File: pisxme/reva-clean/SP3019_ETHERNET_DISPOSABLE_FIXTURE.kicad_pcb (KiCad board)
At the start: 6 copper layers, 300 x 180 mm, 4 parts, among them J2 A70-112-331N126, J7 Raspberry-Pi-5-Compute-Module, U6 SP3019-04HTG, U9 SP3019-04HTG

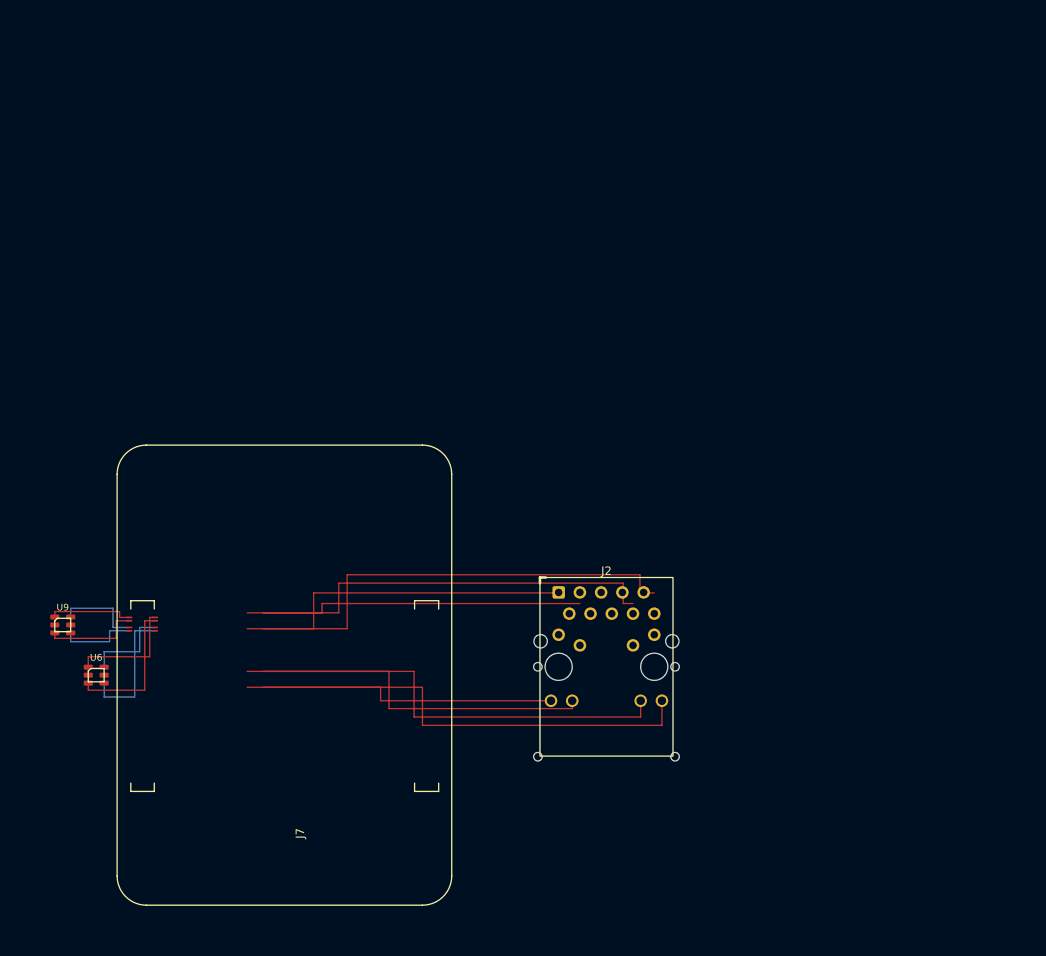
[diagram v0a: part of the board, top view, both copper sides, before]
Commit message: phase17: preserve reoriented Ethernet fixture trial
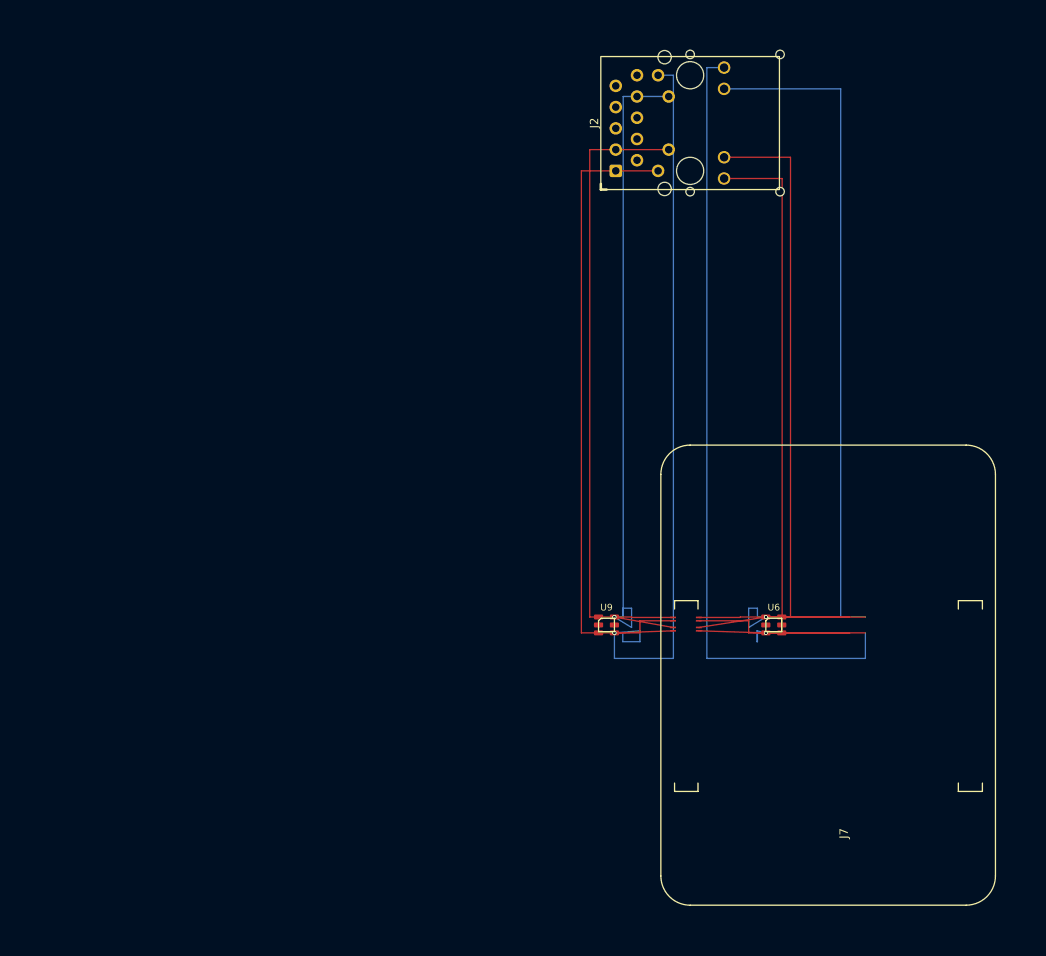
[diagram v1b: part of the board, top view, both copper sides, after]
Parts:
- moved U6 81.2 mm to (110.0, 100.0)
- moved J2 65.8 mm to (100.0, 40.0), turned to 90 degrees
- moved J7 65.0 mm to (100.0, 130.0)
- moved U9 65.0 mm to (90.0, 100.0)
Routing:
- net CM5_GBE_TD0_N: track 52.5 -> 107.8 mm, vias 0 -> 2
- net CM5_GBE_TD0_P: track 81.6 -> 119.1 mm, vias 0 -> 2
- net CM5_GBE_TD1_N: track 55.1 -> 88.8 mm
- net CM5_GBE_TD2_P: track 64.7 -> 97.1 mm, vias 0 -> 2
- net CM5_GBE_TD1_P: track 58.2 -> 88.0 mm
- net CM5_GBE_TD3_P: track 51.1 -> 75.3 mm
- net CM5_GBE_TD3_N: track 53.2 -> 76.8 mm
- net CM5_GBE_TD2_N: track 60.6 -> 83.6 mm, vias 0 -> 2

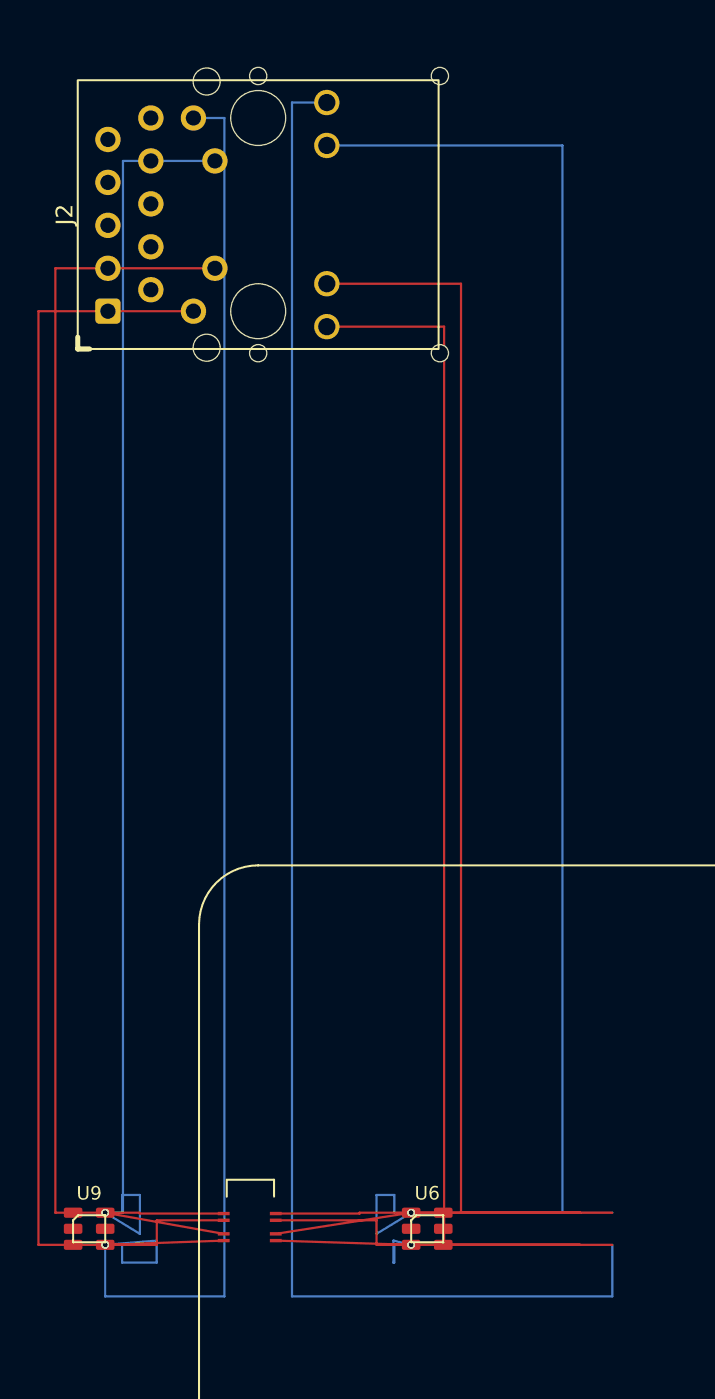
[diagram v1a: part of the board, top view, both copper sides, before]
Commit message: phase17: preserve explicit Ethernet transition trial
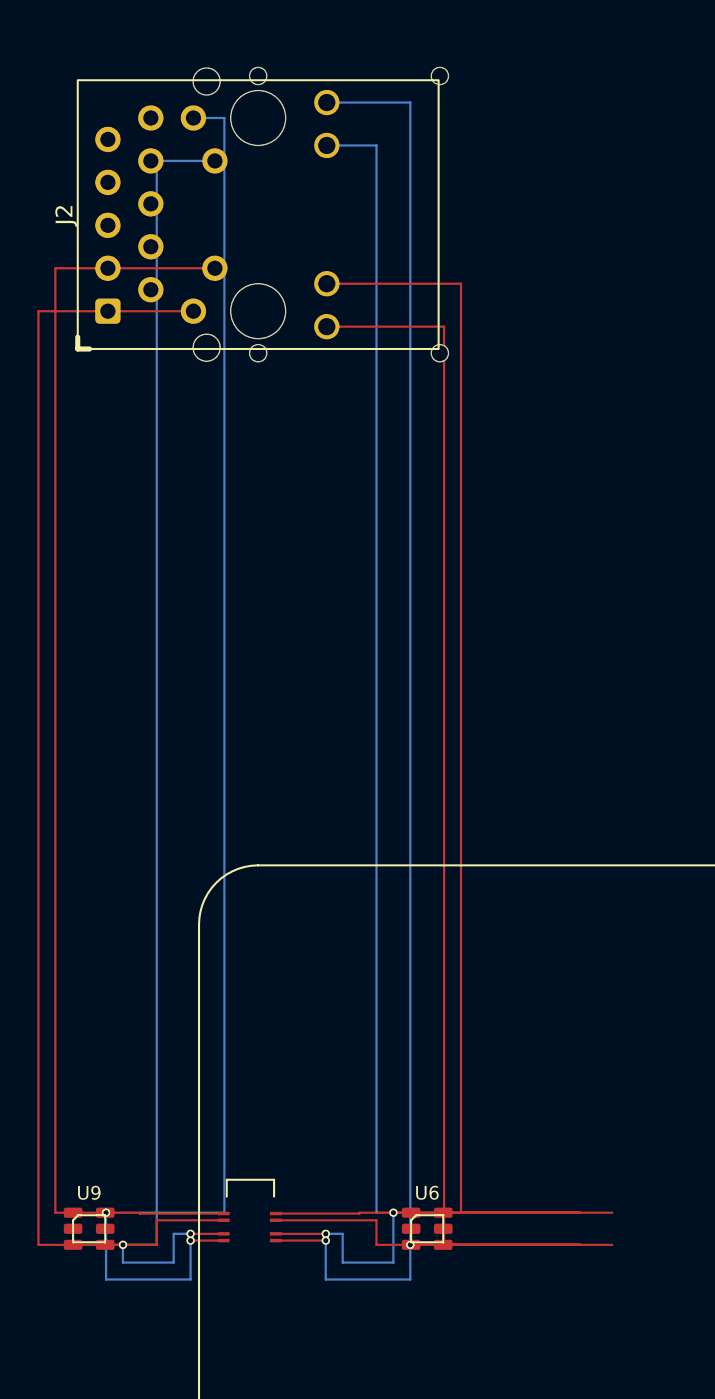
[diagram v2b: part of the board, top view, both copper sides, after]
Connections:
- U6 pad 4: CM5_GBE_TD0_P -> CM5_GBE_TD0_N
- U6 pad 6: CM5_GBE_TD0_N -> CM5_GBE_TD0_P
- U9 pad 4: CM5_GBE_TD2_P -> CM5_GBE_TD2_N
- U9 pad 6: CM5_GBE_TD2_N -> CM5_GBE_TD2_P
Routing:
- net CM5_GBE_TD0_P: track 119.1 -> 96.8 mm
- net CM5_GBE_TD0_N: track 107.8 -> 91.6 mm
- net CM5_GBE_TD2_P: track 97.1 -> 86.9 mm
- net CM5_GBE_TD2_N: track 83.6 -> 79.3 mm

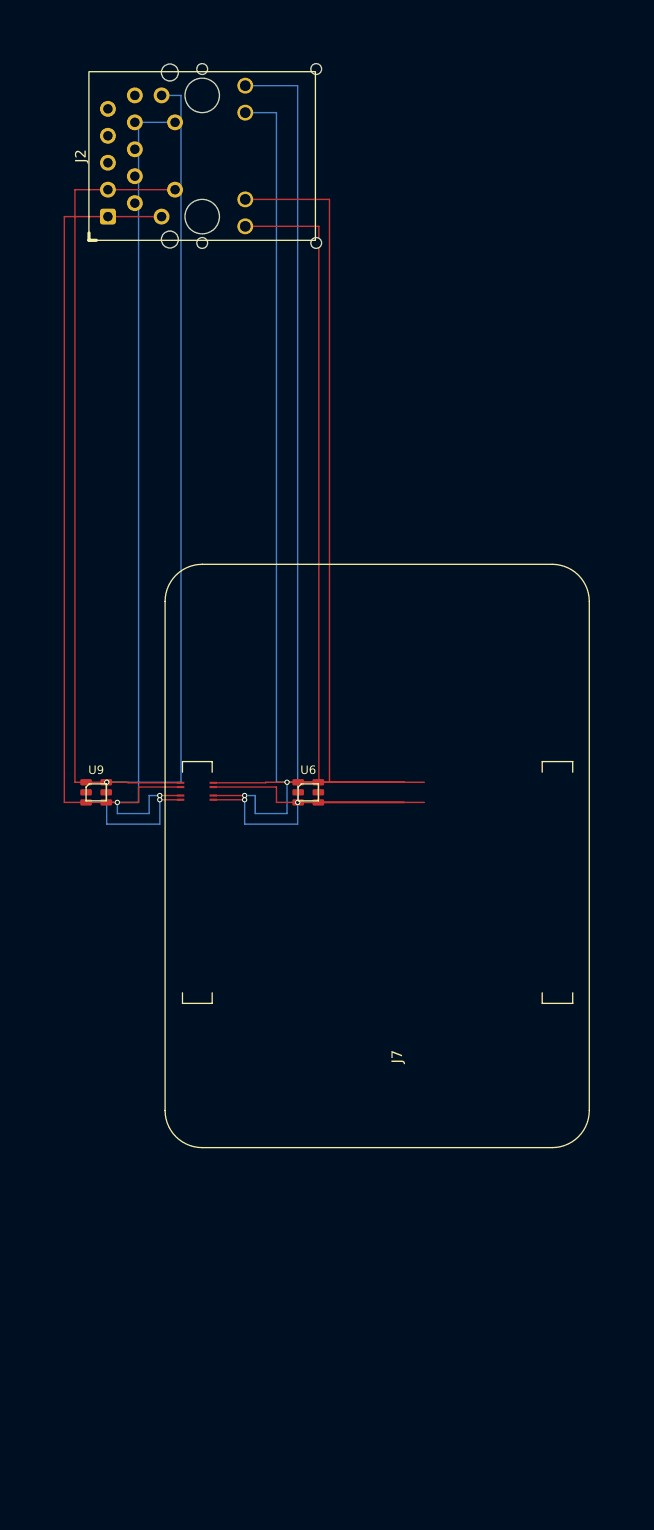
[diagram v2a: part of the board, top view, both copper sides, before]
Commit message: phase17: preserve separated Ethernet placement trial
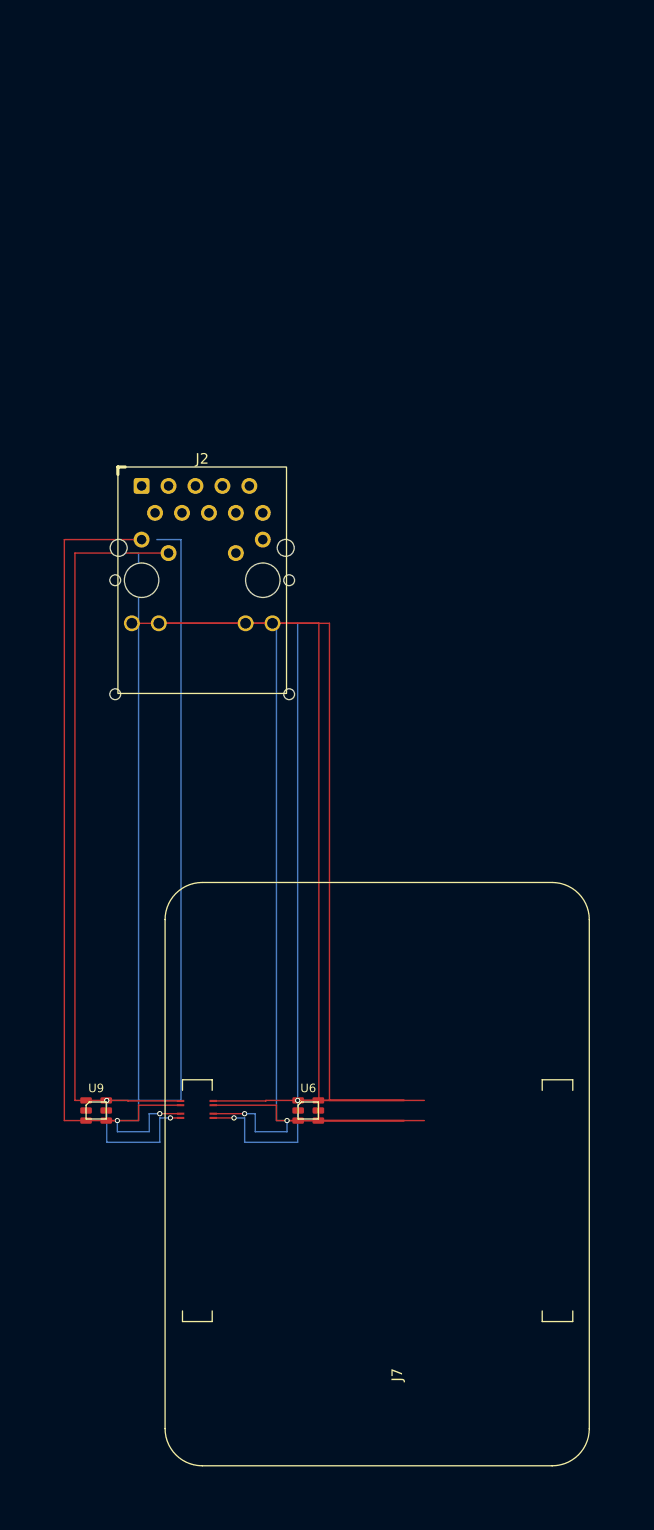
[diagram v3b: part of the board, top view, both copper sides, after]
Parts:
- moved J2 40.0 mm to (100.0, 80.0), turned to 0 degrees
- moved J7 30.0 mm to (100.0, 160.0)
- moved U6 30.0 mm to (110.0, 130.0)
- moved U9 30.0 mm to (90.0, 130.0)
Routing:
- net CM5_GBE_TD0_P: track 96.8 -> 73.5 mm
- net CM5_GBE_TD0_N: track 91.6 -> 73.5 mm
- net CM5_GBE_TD2_N: track 79.3 -> 66.1 mm
- net CM5_GBE_TD2_P: track 86.9 -> 75.4 mm
- net CM5_GBE_TD3_P: track 75.3 -> 70.4 mm
- net CM5_GBE_TD1_N: track 88.8 -> 92.0 mm
- net CM5_GBE_TD3_N: track 76.8 -> 74.5 mm
- net CM5_GBE_TD1_P: track 88.0 -> 86.2 mm

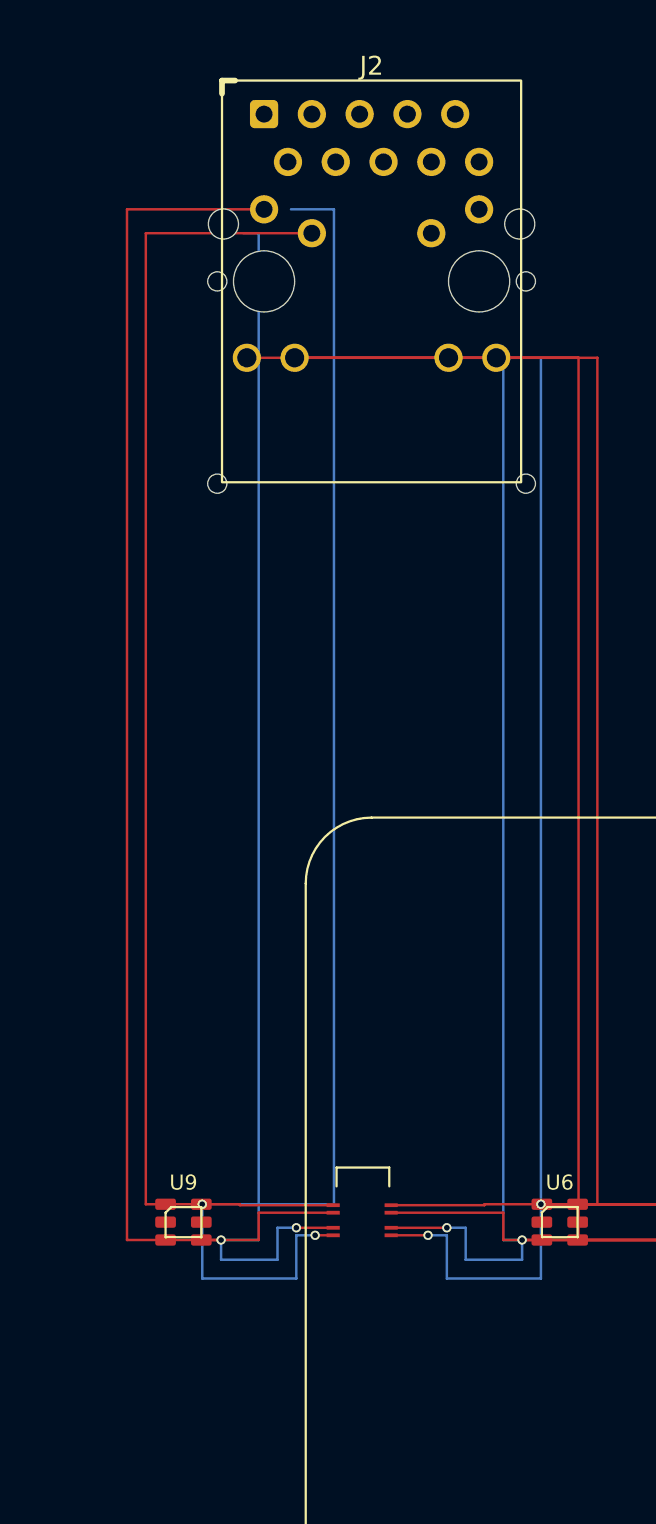
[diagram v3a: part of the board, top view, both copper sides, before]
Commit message: phase17: close disposable Ethernet return path
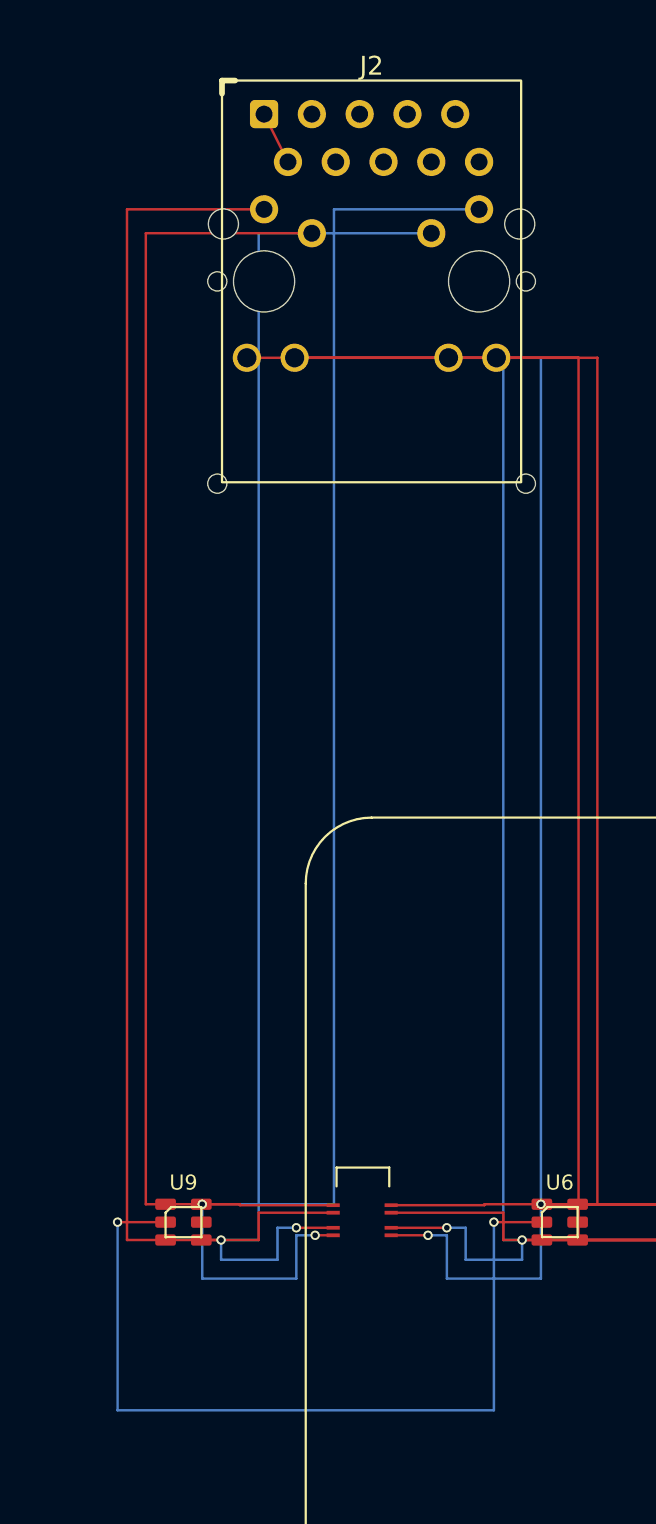
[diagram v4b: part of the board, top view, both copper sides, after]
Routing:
- net /ETHERNET/ETH_GND: track 0.00 -> 45.1 mm, vias 0 -> 2
- net CM5_GBE_TD2_N: track 66.1 -> 74.4 mm
- net CM5_GBE_TD2_P: track 75.4 -> 80.9 mm
- net /ETHERNET/GBE_SHIELD: track 0.00 -> 2.84 mm
